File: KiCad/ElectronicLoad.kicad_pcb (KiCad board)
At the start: 2 copper layers, 99.8 x 99.8 mm, 182 parts, among them J1 LOAD, J2 SMA2, J3 SMA1, J4 12V, J5 USB, J6 PROG, M1 FAN, Q1 any, Q2 any, Q3 BSS138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

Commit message: rev0.2: remove DAC offset compensation and test connectors
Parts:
- removed C12, C13: nc, Capacitor_SMD:C_0805_2012Metric
- removed J2: SMA2, Library:SMA_Amphenol_901-143_Horizontal
- removed J3: SMA1, Library:SMA_Amphenol_901-143_Horizontal
- removed R49, R50, R51, R52, R53, R54, R55, R56, R57, R58: nc, Resistor_SMD:R_0805_2012Metric
- removed R71, R73, R77, R78: 2k, Resistor_SMD:R_0603_1608Metric
- removed R72, R76: 20k, Resistor_SMD:R_0603_1608Metric
- removed RV1, RV2: 2k, Library-RV:PVG3A
- C1, C2: value C_Small -> 1nF (tbd)
- C11: value tdb -> 22pF (tbd)
- C14, C15: value tbd -> dnp*
- C16, C20, C21: value tbd -> 100pF (tbd)
- C17: value tb -> 100pF (tbd)
- C19: value tbd -> 3.3pF (tbd)
- R10, R9: value 220 -> 330
- R40, R42: value 50k* -> 33k (1%)
- R46: value tbd -> 47k*
- R47: value tbd -> 1k*
- R48: value 1k -> 10k
- R66: value 220 -> 2.2k
- R67: value 330 -> 3.3k
- R68: value 2k -> 12k
- R74, R80: value tbd -> 20k
- R75, R79: value tbd -> 10k
- R95: value 10 -> 1ohm
- R96: value 10 -> dnp
- R98, R99: value 10k* -> 10k (1%)
- U1, U2, U6: value LM2904 -> opamp
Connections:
- U6 pad 3: Net-(U6A-+) -> I1_set
- U6 pad 5: Net-(U6B-+) -> I2_set
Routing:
- net /PWR_SET_AMP: track 72.4 -> 46.3 mm, vias 4 -> 2
- net Net-(R78-Pad1): track 11.8 -> 0.00 mm
- net Net-(R73-Pad1): track 11.6 -> 0.00 mm
- net Net-(J2-In): track 9.48 -> 0.00 mm
- net Net-(J3-In): track 9.47 -> 0.00 mm
- net Net-(R49-Pad2): track 8.05 -> 0.00 mm
- net Net-(C13-Pad1): track 6.81 -> 0.00 mm
- net Net-(C12-Pad1): track 6.32 -> 0.00 mm
- net Net-(R52-Pad2): track 5.62 -> 0.00 mm
- net Net-(R76-Pad1): track 5.20 -> 0.00 mm
- net Net-(U6B-+): track 3.51 -> 0.00 mm
- net Net-(U6A-+): track 3.48 -> 0.00 mm
- net Net-(R72-Pad1): track 1.89 -> 0.00 mm
- net I2_set: track 44.4 -> 45.7 mm
- net I1_set: track 59.6 -> 59.1 mm

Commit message: rev0.2: use only one Current Set line
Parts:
- removed C20: 100pF (tbd), Capacitor_SMD:C_0603_1608Metric
- removed D10: 12V, Diode_SMD:D_SOD-323_HandSoldering
- removed R41: 1k, Resistor_SMD:R_0603_1608Metric
- removed R43, R82: 0, Resistor_SMD:R_0603_1608Metric
- removed R79: 10k, Resistor_SMD:R_0603_1608Metric
- removed R80: 20k, Resistor_SMD:R_0603_1608Metric
- removed R92: R_Small, Resistor_SMD:R_0603_1608Metric
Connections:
- net I1_set renamed I_set
- net I1_set_amp renamed I_set_amp
- R39 pad 2: /I1_set_a -> /I_set_a
- U2 pad 3: /I1_set_a -> /I_set_a
- U2 pad 5: /I2_set_a -> /I_set_a
- U5 pad 10: Net-(U5-GPIO17/U1TXD/ADC2_CH6/DAC_1) -> unconnected-(U5-GPIO17/U1TXD/ADC2_CH6/DAC_1-Pad10)
- U6 pad 5: I2_set -> unconnected-(U6B-+-Pad5)
- U6 pad 6: Net-(U6B--) -> unconnected-(U6B---Pad6)
- U6 pad 7: Net-(R80-Pad2) -> unconnected-(U6-Pad7)
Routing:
- net /I_set_a: track 0.00 -> 51.5 mm, vias 0 -> 3
- net /I1_set_a: track 47.3 -> 0.00 mm, vias 2 -> 0
- net I2_set: track 45.7 -> 0.00 mm, vias 2 -> 0
- net /I2_set_a: track 38.2 -> 0.00 mm, vias 2 -> 0
- net I2_set_amp: track 34.8 -> 0.00 mm, vias 2 -> 0
- net Net-(U6B--): track 5.18 -> 0.00 mm
- net Net-(R80-Pad2): track 4.53 -> 0.00 mm
- net Net-(U5-GPIO17/U1TXD/ADC2_CH6/DAC_1): track 2.05 -> 0.00 mm
- net Net-(C19-Pad1): track 6.85 -> 5.04 mm

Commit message: rev0.2: separate DAC10/11 lines from RX/TX
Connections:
- J6 pad 2: DAC_11 -> /TX
- J6 pad 3: DAC_10 -> /RX
- U5 pad 20: unconnected-(U5-GPIO12/TOUCH12/ADC2_CH1/FSPICLK/FSPIIO6-Pad20) -> DAC_11
- U5 pad 21: unconnected-(U5-GPIO13/TOUCH13/ADC2_CH2/FSPIQ/FSPIIO7-Pad21) -> DAC_10
- U5 pad 36: DAC_10 -> /RX
- U5 pad 37: DAC_11 -> /TX
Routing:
- net /TX: track 0.00 -> 37.8 mm, vias 0 -> 1
- net /RX: track 0.00 -> 36.1 mm, vias 0 -> 1
- net DAC_10: track 58.7 -> 39.0 mm
- net DAC_11: track 58.0 -> 38.4 mm
- net BTN: track 81.9 -> 83.9 mm
- net LED: track 75.6 -> 77.4 mm
- net /PWR_SET_AMP: track 46.3 -> 47.5 mm
- net GND: vias 128 -> 123

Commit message: rev0.2: remove MOSFET caps
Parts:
- removed C14, C15: dnp*, Capacitor_SMD:C_0603_1608Metric
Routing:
- net Net-(C1-Pad2): track 11.2 -> 9.61 mm

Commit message: rev0.2: redesign the Voltage & (MCU) Current Sense circuits
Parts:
- removed C16, C17: 100pF (tbd), Capacitor_SMD:C_0603_1608Metric
- removed D11, D12: 12V, Diode_SMD:D_SOD-323_HandSoldering
- removed R98, R99: 10k (1%), Resistor_SMD:R_0603_1608Metric
- added C12: 22pF (tbd), Capacitor_SMD:C_0603_1608Metric, B.Cu at (114.8, 73.8)
- added C13: 22pF (tbd), Capacitor_SMD:C_0603_1608Metric, B.Cu at (127.4, 83.3)
- added C14: 22pF (tbd), Capacitor_SMD:C_0603_1608Metric, B.Cu at (127.5, 80.3)
- added C15: 1u, Capacitor_SMD:C_0603_1608Metric, B.Cu at (105.6, 135.9)
- added D10: 3.3V, Diode_SMD:D_SOD-323_HandSoldering, B.Cu at (110.9, 143.3)
- added R41: 0*, Resistor_SMD:R_0603_1608Metric, B.Cu at (118.8, 147.6)
- added R43: 22, Resistor_SMD:R_0603_1608Metric, B.Cu at (103.2, 136.3)
- added R49: 1M, Resistor_SMD:R_0603_1608Metric, B.Cu at (112.9, 143.9)
- added R50: 22, Resistor_SMD:R_0603_1608Metric, B.Cu at (130.5, 83.3)
- added R51: 22, Resistor_SMD:R_0603_1608Metric, B.Cu at (130.5, 80.3)
- added R52: 22, Resistor_SMD:R_0603_1608Metric, B.Cu at (129.0, 80.3)
- added R53: 22, Resistor_SMD:R_0603_1608Metric, B.Cu at (129.0, 83.3)
- added U7: opamp, Package_SO:SOIC-8_3.9x4.9mm_P1.27mm, B.Cu at (110.9, 137.6)
- added U8: opamp, Package_SO:SOIC-8_3.9x4.9mm_P1.27mm, F.Cu at (146.9, 116.8)
- C11: footprint Capacitor_SMD:C_0805_2012Metric -> Capacitor_SMD:C_0603_1608Metric
- R40, R42: value 33k (1%) -> 1M; moved to F.Cu
- R44: value 0 -> 1M
- R46: value 47k* -> 470k*; footprint Resistor_SMD:R_0805_2012Metric -> Resistor_SMD:R_0603_1608Metric
- R47: value 1k* -> 10k*; footprint Resistor_SMD:R_0805_2012Metric -> Resistor_SMD:R_0603_1608Metric
- R48: value 10k -> 22; footprint Resistor_SMD:R_0805_2012Metric -> Resistor_SMD:R_0603_1608Metric
- R64: moved to F.Cu
- U6: footprint Package_SO:SOIC-8_3.9x4.9mm_P1.27mm -> Package_TO_SOT_SMD:SOT-23-5
- moved R44 69.2 mm to (115.6, 143.9), turned to -90 degrees
- moved C11 65.7 mm to (113.2, 73.8), turned to 90 degrees
- moved R42 43.6 mm to (147.8, 120.3), turned to 180 degrees
- moved R40 39.7 mm to (144.7, 120.3), turned to 0 degrees
- moved R17 15.8 mm to (102.6, 106.3)
- moved R32 15.8 mm to (102.6, 109.5)
- moved R16 12.1 mm to (104.5, 106.3), turned to -90 degrees
- moved C19 11.7 mm to (113.1, 109.5), turned to -90 degrees
- moved R70 10.4 mm to (113.0, 103.1), turned to 90 degrees
- moved R15 10.3 mm to (106.2, 106.3), turned to -90 degrees
- moved R46 10.2 mm to (114.8, 147.5)
- moved R47 9.99 mm to (110.8, 147.6), turned to 0 degrees
- moved D1 9.91 mm to (117.5, 143.4)
- moved R33 9.15 mm to (104.5, 109.5), turned to 90 degrees
- moved R14 8.87 mm to (108.0, 106.2), turned to -90 degrees
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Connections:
- C1 pad 1: /I1_amp_a -> Net-(U2A--)
- C11 pad 1: V_LOAD_SEN -> V_LOAD_SEN_1
- C2 pad 1: /I2_amp_a -> Net-(U2B--)
- D1 pad 2: V_LOAD_SEN -> Net-(D1-A2)
- R10 pad 1: Net-(R10-Pad1) -> /I2_amp_a
- R10 pad 2: /I2_amp_a -> Net-(U2B--)
- R2 pad 1: Net-(R10-Pad1) -> /I2_amp_a
- R40 pad 1: I1_amp -> /I1_amp_a
- R40 pad 2: /I1_amp_a -> Net-(U8A-+)
- R42 pad 2: I2_amp -> Net-(U8B-+)
- R44 pad 1: I_set -> Net-(D1-A2)
- R44 pad 2: Net-(U5-GPIO18/U1RXD/ADC2_CH7/DAC_2/CLK_OUT3) -> Net-(R41-Pad1)
- R46 pad 2: V_LOAD -> Net-(R41-Pad1)
- R48 pad 1: V_LOAD_SEN -> V_LOAD_SEN_1
- R48 pad 2: Net-(R46-Pad1) -> Net-(U7A--)
- R5 pad 1: Net-(R5-Pad1) -> /I1_amp_a
- R74 pad 1: Net-(U6A--) -> Net-(U6--)
- R75 pad 2: Net-(U6A--) -> Net-(U6--)
- R9 pad 1: /I1_amp_a -> Net-(U2A--)
- R9 pad 2: Net-(R5-Pad1) -> /I1_amp_a
- U1 pad 1: Net-(R5-Pad1) -> /I1_amp_a
- U1 pad 7: Net-(R10-Pad1) -> /I2_amp_a
- U2 pad 2: /I1_amp_a -> Net-(U2A--)
- U2 pad 6: /I2_amp_a -> Net-(U2B--)
- U5 pad 11: Net-(U5-GPIO18/U1RXD/ADC2_CH7/DAC_2/CLK_OUT3) -> unconnected-(U5-GPIO18/U1RXD/ADC2_CH7/DAC_2/CLK_OUT3-Pad11)
- U5 pad 20: DAC_11 -> DAC_10
- U5 pad 21: DAC_10 -> DAC_11
- U5 pad 33: DAC_7 -> DAC_13
- U5 pad 34: DAC_8 -> DAC_12
- U5 pad 38: DAC_12 -> DAC_8
- U5 pad 39: DAC_13 -> DAC_7
- U5 pad 6: V_LOAD_SEN -> V_LOAD_SEN_1
- U5 pad 7: unconnected-(U5-GPIO7/TOUCH7/ADC1_CH6-Pad7) -> V_LOAD_SEN_2
- U6 pad 2: Net-(U6A--) -> GND
- U6 pad 4: GND -> Net-(U6--)
- U6 pad 5: unconnected-(U6B-+-Pad5) -> /PWR_SET_AMP
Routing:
- net V_LOAD_SEN_1: track 0.00 -> 76.1 mm, vias 0 -> 2
- net V_LOAD_SEN: track 72.3 -> 0.00 mm, vias 2 -> 0
- net V_LOAD_SEN_2: track 0.00 -> 68.4 mm, vias 0 -> 2
- net /I2_buf: track 0.00 -> 66.6 mm, vias 0 -> 1
- net I_set: track 59.5 -> 4.10 mm, vias 2 -> 0
- net /I1_buf: track 0.00 -> 53.5 mm, vias 0 -> 1
- net /I2_amp_a: track 69.3 -> 20.3 mm, vias 2 -> 1
- net /I1_amp_a: track 59.1 -> 11.8 mm, vias 2 -> 1
- net /PWR_SET_AMP: track 47.5 -> 91.0 mm, vias 2 -> 3
- net DAC_7: track 36.4 -> 15.4 mm
- net DAC_8: track 32.3 -> 15.4 mm
- net DAC_11: track 38.4 -> 27.8 mm
- net Net-(U2B--): track 0.00 -> 10.4 mm
- net DAC_10: track 39.0 -> 29.6 mm
- net DAC_9: track 26.7 -> 17.5 mm
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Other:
- board text added: "(v0.2)"
- board text removed: "(v0.1)"

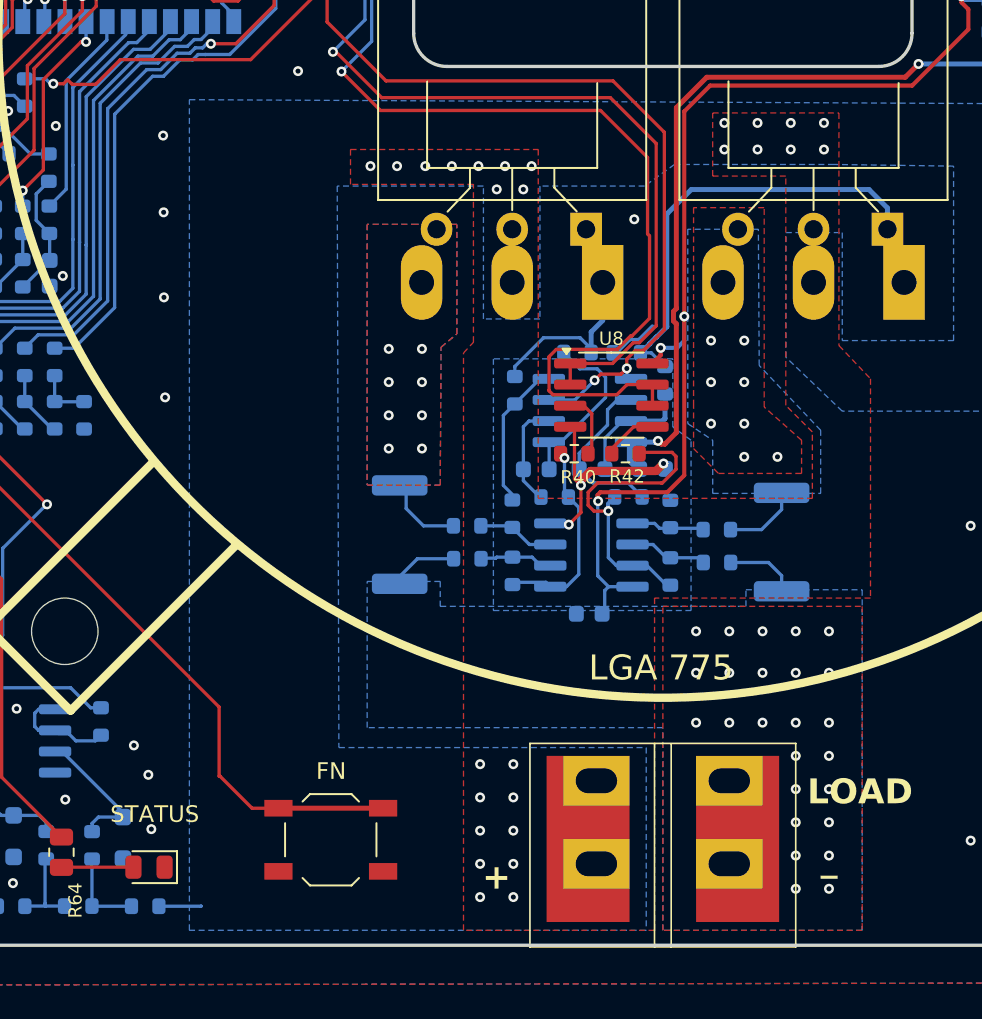
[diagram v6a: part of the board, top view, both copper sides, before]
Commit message: rev0.2: add duplicate current sense resistor footprint
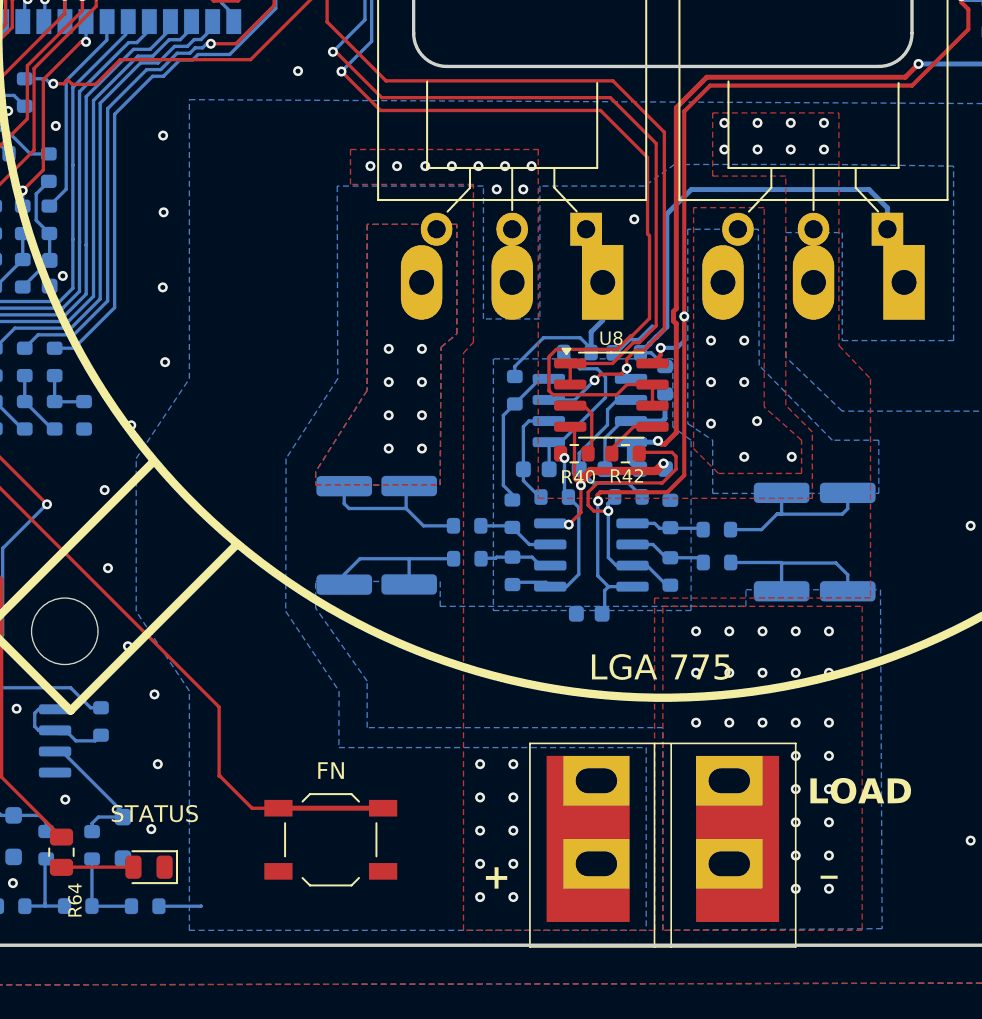
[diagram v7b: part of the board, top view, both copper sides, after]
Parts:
- added RS3: 0.001, Resistor_SMD:R_2512_6332Metric, B.Cu at (130.8, 125.2)
- added RS4: 0.001, Resistor_SMD:R_2512_6332Metric, B.Cu at (161.1, 125.6)
- R39: value 1k -> 22
- moved REF** 29.7 mm to (187.1, 99.8)
- moved REF** 29.7 mm to (187.2, 115.9)
- moved RS1 0.57 mm to (134.7, 125.2)
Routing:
- net GND: track 34.8 -> 45.5 mm, vias 120 -> 124
- net Net-(Q2-S): track 4.58 -> 10.1 mm
- net Net-(Q1-S): track 4.19 -> 9.09 mm
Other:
- board text added: "Volt Sense"

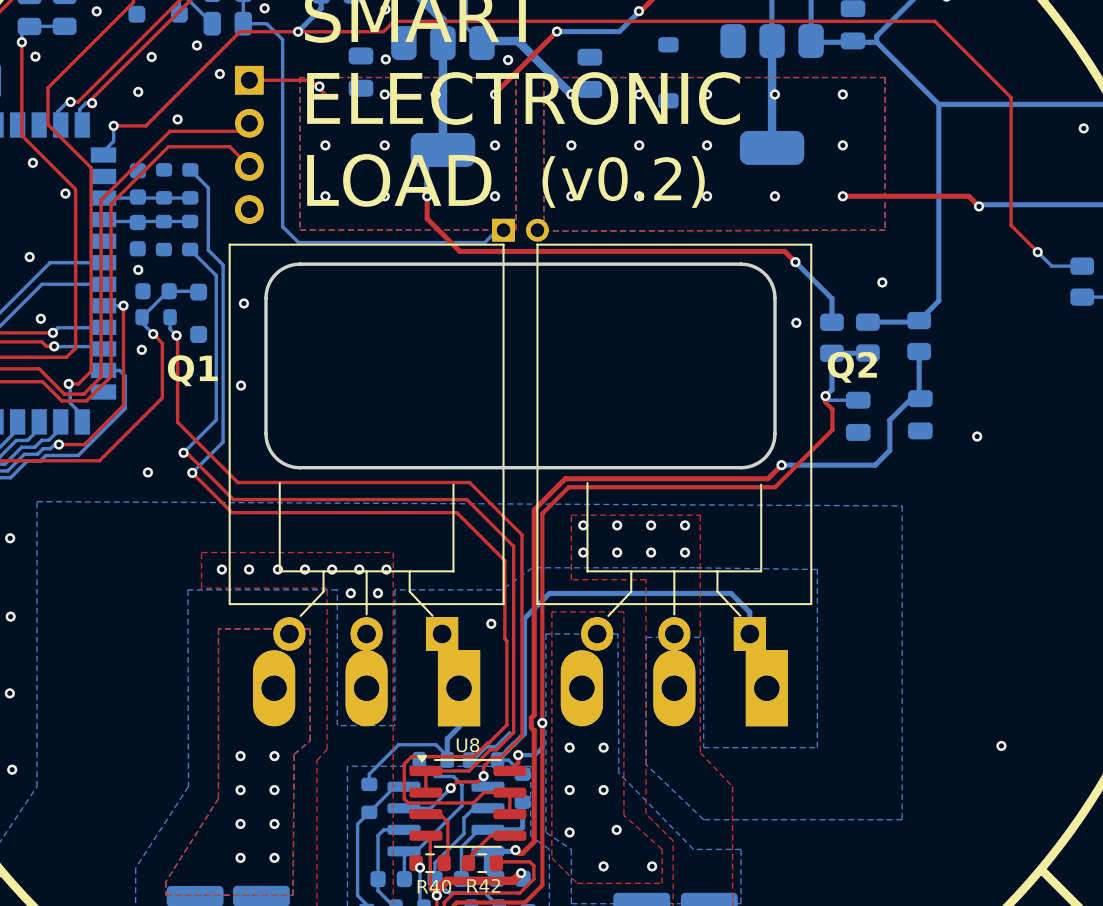
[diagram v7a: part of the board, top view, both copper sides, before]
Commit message: rev0.2: add disable MOSFET-s signal
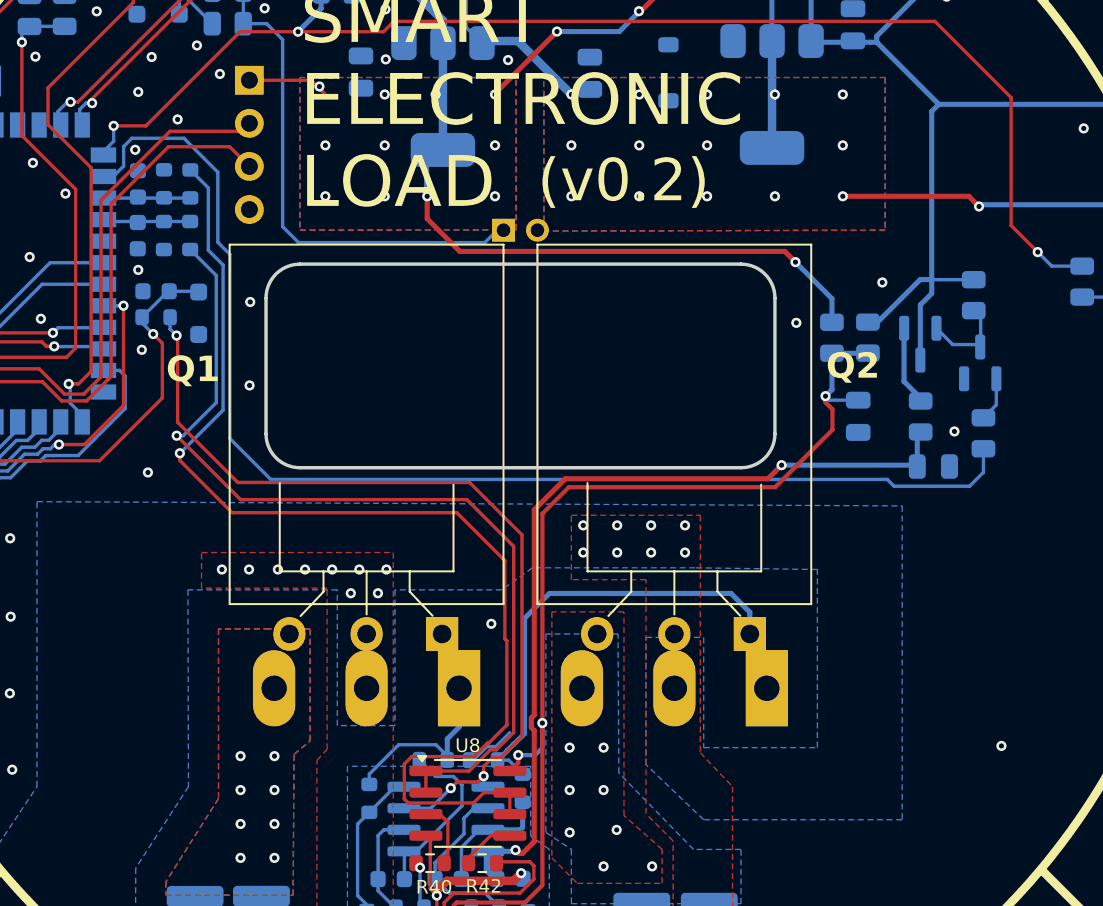
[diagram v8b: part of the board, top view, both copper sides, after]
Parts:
- added Q4: PMOS, Package_TO_SOT_SMD:SOT-23, B.Cu at (173.6, 89.7)
- added Q5: BSS138, Package_TO_SOT_SMD:SOT-23, B.Cu at (177.1, 90.8)
- added R54: 10k, Resistor_SMD:R_0805_2012Metric, B.Cu at (176.7, 86.8)
- added R55: 22, Resistor_SMD:R_0805_2012Metric, B.Cu at (177.3, 95.0)
- moved R91 4.74 mm to (173.6, 94.0)
- moved REF** 3.83 mm to (186.6, 103.6)
- moved REF** 3.26 mm to (186.8, 119.1)
- moved C27 3.15 mm to (174.3, 96.9), turned to 0 degrees
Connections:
- R91 pad 2: +12V -> Net-(Q4-D)
- U5 pad 16: unconnected-(U5-GPIO46-Pad16) -> PWR_C_SET_EN
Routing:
- net PWR_C_SET_EN: track 0.00 -> 72.5 mm
- net +12V: track 130.5 -> 137.0 mm
- net Net-(Q4-G): track 0.00 -> 5.17 mm
- net Net-(Q4-D): track 0.00 -> 4.73 mm
- net /PWR_C_SET: track 54.0 -> 50.5 mm
- net Net-(Q5-G): track 0.00 -> 2.61 mm
- net /I2_buf: track 66.6 -> 67.2 mm
- net GND: vias 124 -> 125
